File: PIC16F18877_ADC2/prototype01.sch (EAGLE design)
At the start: 39 parts, among them CN1 12V_IN, CN10 PIC_PORTD_IF, CN2 PIC_PORTA_IF, CN3 UART_IF, CN4 PIC_CN_H, CN5 AE-MICRO-SD-DIP, CN6 I2C_IF, CN7 PIC_PORTB_IF, CN8 PIC_PORTE_IF, CN9 PIC_PORTC_IF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

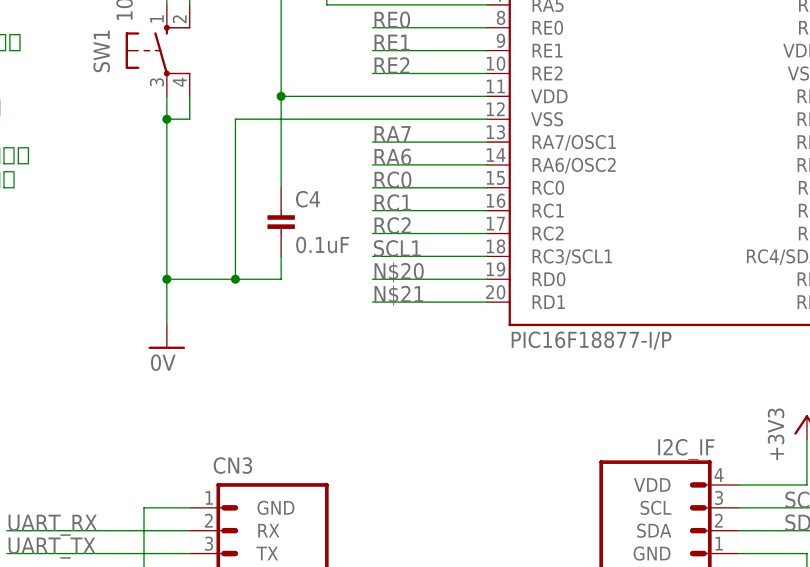
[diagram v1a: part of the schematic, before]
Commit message: 部品配置を修正
LEDの位置をピンのそばに移動
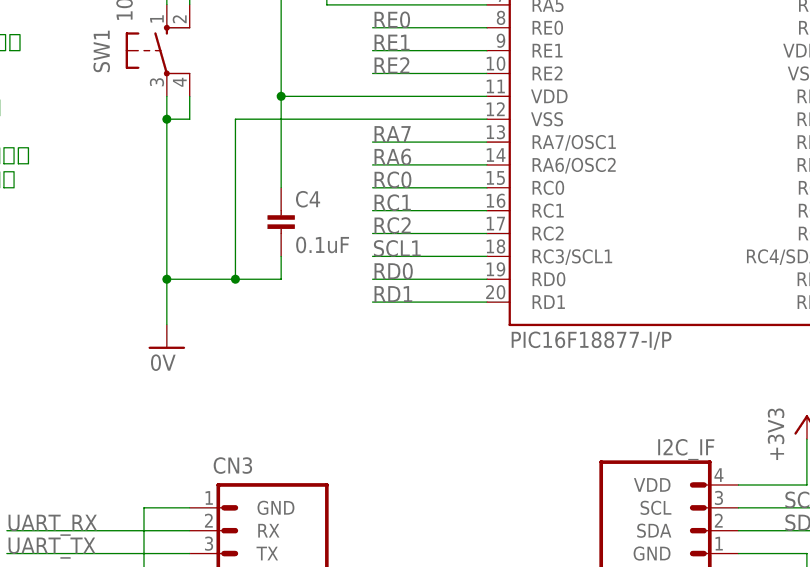
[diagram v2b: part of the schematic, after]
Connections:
- removed net N$20: U2.RD0
- removed net N$21: U2.RD1
- net RD0: now also U2.RD0
- net RD1: now also U2.RD1
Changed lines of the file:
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@@
 <label x="210.82" y="58.42" size="1.778" layer="95"/>
+</segment>
+<segment>
+<pinref part="U2" gate="G$1" pin="RD0"/>
+<wire x1="165.1" y1="144.78" x2="152.4" y2="144.78" width="0.1524" layer="91"/>
+<label x="152.4" y="144.78" size="1.778" layer="95"/>
 </segment>
 </net>
@@
 <wire x1="220.98" y1="60.96" x2="210.82" y2="60.96" width="0.1524" layer="91"/>
 <label x="210.82" y="60.96" size="1.778" layer="95"/>
+</segment>
+<segment>
+<pinref part="U2" gate="G$1" pin="RD1"/>
+<wire x1="165.1" y1="142.24" x2="152.4" y2="142.24" width="0.1524" layer="91"/>
+<label x="152.4" y="142.24" size="1.778" layer="95"/>
 </segment>
 </net>
@@
 </segment>
 </net>
-<net name="N$20" class="0">
-<segment>
-<pinref part="U2" gate="G$1" pin="RD0"/>
-<wire x1="165.1" y1="144.78" x2="152.4" y2="144.78" width="0.1524" layer="91"/>
-<label x="152.4" y="144.78" size="1.778" layer="95"/>
-</segment>
-</net>
-<net name="N$21" class="0">
-<segment>
-<pinref part="U2" gate="G$1" pin="RD1"/>
-<wire x1="165.1" y1="142.24" x2="152.4" y2="142.24" width="0.1524" layer="91"/>
-<label x="152.4" y="142.24" size="1.778" layer="95"/>
-</segment>
-</net>
